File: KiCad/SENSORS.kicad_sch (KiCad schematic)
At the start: 0 parts

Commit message: Canvis a sensors
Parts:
- added D1: LED, symbol Device:LED
- added U1: TMP102xxDRL, Package_TO_SOT_SMD:SOT-563, symbol Sensor_Temperature:TMP102xxDRL
- added U2: A1104xLH, Package_TO_SOT_SMD:SOT-23W, symbol Sensor_Magnetic:A1104xLH
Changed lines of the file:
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@@
 	(generator_version "9.0")
 	(paper "A4")
+	(symbol
+		(lib_id "Sensor_Temperature:TMP102xxDRL")
+		(at 139.7 77.47 0)
+		(unit 1)
+		(exclude_from_sim no)
+		(in_bom yes)
+		(on_board yes)
+		(dnp no)
+		(fields_autoplaced yes)
+		(property "Reference" "U1"
+			(at 154.94 65.9698 0)
+			(effects
+				(font
+					(size 1.27 1.27)
+				)
+			)
+		)
+		(property "Value" "TMP102xxDRL"
+			(at 154.94 68.5098 0)
+			(effects
+				(font
+					(size 1.27 1.27)
+				)
+			)
+		)
+		(property "Footprint" "Package_TO_SOT_SMD:SOT-563"
+			(at 140.97 86.36 0)
+			(effects
+				(font
+					(size 1.27 1.27)
+				)
+				(justify left)
+				(hide yes)
+			)
+		)
+		(property "Datasheet" "https://www.ti.com/lit/ds/symlink/tmp102.pdf"
+			(at 140.97 88.9 0)
+			(effects
+				(font
+					(size 1.27 1.27)
+				)
+				(justify left)
+				(hide yes)
+			)
+		)
+		(property "Description" "Digital Temperature Sensor, ±3°C, low-Power, SMBus, 12 bit, Two-Wire Serial Interface, SOT-563"
+			(at 139.7 77.47 0)
+			(effects
+				(font
+					(size 1.27 1.27)
+				)
+				(hide yes)
+			)
+		)
+		(pin "4"
+		)
+		(pin "3"
+		)
+		(pin "5"
+		)
+		(pin "2"
+		)
+		(pin "1"
+		)
+		(pin "6"
+		)
+		(instances
+			(project ""
+				(path "/264905d4-7c45-4183-babb-a5b2177ba886"
+					(reference "U1")
+					(unit 1)
+				)
+			)
+		)
+	)
+	(symbol
+		(lib_id "Device:LED")
+		(at 166.37 107.95 0)
+		(unit 1)
+		(exclude_from_sim no)
+		(in_bom yes)
+		(on_board yes)
+		(dnp no)
+		(fields_autoplaced yes)
+		(property "Reference" "D1"
+			(at 164.7825 101.6 0)
+			(effects
+				(font
+					(size 1.27 1.27)
+				)
+			)
+		)
+		(property "Value" "LED"
+			(at 164.7825 104.14 0)
+			(effects
+				(font
+					(size 1.27 1.27)
+				)
+			)
+		)
+		(property "Footprint" ""
+			(at 166.37 107.95 0)
+			(effects
+				(font
+					(size 1.27 1.27)
+				)
+				(hide yes)
+			)
+		)
+		(property "Datasheet" "~"
+			(at 166.37 107.95 0)
+			(effects
+				(font
+					(size 1.27 1.27)
+				)
+				(hide yes)
+			)
+		)
+		(property "Description" "Light emitting diode"
+			(at 166.37 107.95 0)
+			(effects
+				(font
+					(size 1.27 1.27)
+				)
+				(hide yes)
+			)
+		)
+		(property "Sim.Pins" "1=K 2=A"
+			(at 166.37 107.95 0)
+			(effects
+				(font
+					(size 1.27 1.27)
+				)
+				(hide yes)
+			)
+		)
+		(pin "1"
+		)
+		(pin "2"
+		)
+		(instances
+			(project ""
+				(path "/264905d4-7c45-4183-babb-a5b2177ba886"
+					(reference "D1")
+					(unit 1)
+				)
+			)
+		)
+	)
+	(symbol
+		(lib_id "Sensor_Magnetic:A1104xLH")
+		(at 139.7 121.92 0)
+		(unit 1)
+		(exclude_from_sim no)
+		(in_bom yes)
+		(on_board yes)
+		(dnp no)
+		(fields_autoplaced yes)
+		(property "Reference" "U2"
+			(at 133.35 120.6499 0)
+			(effects
+				(font
+					(size 1.27 1.27)
+				)
+				(justify right)
+			)
+		)
+		(property "Value" "A1104xLH"
+			(at 133.35 123.1899 0)
+			(effects
+				(font
+					(size 1.27 1.27)
+				)
+				(justify right)
+			)
+		)
+		(property "Footprint" "Package_TO_SOT_SMD:SOT-23W"
+			(at 139.7 139.192 0)
+			(effects
+				(font
+					(size 1.27 1.27)
+					(italic yes)
+				)
+				(hide yes)
+			)
+		)
+		(property "Datasheet" "https://www.allegromicro.com/-/media/files/datasheets/a110x-datasheet.ashx"
+			(at 139.7 134.62 0)
+			(effects
+				(font
+					(size 1.27 1.27)
+				)
+				(hide yes)
+			)
+		)
+		(property "Description" "Hall effect switch, unipolar (south-polarity), Bop=70-350G, Brp=50-330G, 3.8-24V supply, SOT-23W"
+			(at 139.7 136.906 0)
+			(effects
+				(font
+					(size 1.27 1.27)
+				)
+				(hide yes)
+			)
+		)
+		(pin "2"
+		)
+		(pin "1"
+		)
+		(pin "3"
+		)
+		(instances
+			(project ""
+				(path "/264905d4-7c45-4183-babb-a5b2177ba886"
+					(reference "U2")
+					(unit 1)
+				)
+			)
+		)
+	)
+	(sheet_instances
+		(path "/"
+			(page "1")
+		)
+	)
+	(embedded_fonts no)
 )

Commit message: Canvis a SENSORS
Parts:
- added R1: R, symbol Device:R
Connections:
- net at D1.1 (K): now also R1.1
- net at U2.2 (V_{OUT}): now also R1.2
- net GND: now reaches U2.3 (GND)
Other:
- moved on the sheet: D1, U1
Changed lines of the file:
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@@
 	(generator_version "9.0")
 	(paper "A4")
+	(wire
+		(pts
+			(xy 147.32 121.92) (xy 152.4 121.92)
+		)
+		(stroke
+			(width 0)
+			(type default)
+		)
+	)
+	(wire
+		(pts
+			(xy 137.16 132.08) (xy 137.16 135.89)
+		)
+		(stroke
+			(width 0)
+			(type default)
+		)
+	)
+	(wire
+		(pts
+			(xy 152.4 121.92) (xy 152.4 115.57)
+		)
+		(stroke
+			(width 0)
+			(type default)
+		)
+	)
+	(wire
+		(pts
+			(xy 152.4 101.6) (xy 152.4 107.95)
+		)
+		(stroke
+			(width 0)
+			(type default)
+		)
+	)
 	(symbol
 		(lib_id "Sensor_Temperature:TMP102xxDRL")
-		(at 139.7 77.47 0)
+		(at 110.49 41.91 0)
 		(unit 1)
 		(exclude_from_sim no)
@@
 		(fields_autoplaced yes)
 		(property "Reference" "U1"
-			(at 154.94 65.9698 0)
+			(at 125.73 30.4098 0)
 			(effects
 				(font
@@
 		)
 		(property "Value" "TMP102xxDRL"
-			(at 154.94 68.5098 0)
+			(at 125.73 32.9498 0)
 			(effects
 				(font
@@
 		)
 		(property "Footprint" "Package_TO_SOT_SMD:SOT-563"
-			(at 140.97 86.36 0)
+			(at 111.76 50.8 0)
 			(effects
 				(font
@@
 		)
 		(property "Datasheet" "https://www.ti.com/lit/ds/symlink/tmp102.pdf"
-			(at 140.97 88.9 0)
+			(at 111.76 53.34 0)
 			(effects
 				(font
@@
 		)
 		(property "Description" "Digital Temperature Sensor, ±3°C, low-Power, SMBus, 12 bit, Two-Wire Serial Interface, SOT-563"
-			(at 139.7 77.47 0)
+			(at 110.49 41.91 0)
 			(effects
 				(font
@@
 	(symbol
 		(lib_id "Device:LED")
-		(at 166.37 107.95 0)
+		(at 152.4 97.79 90)
 		(unit 1)
 		(exclude_from_sim no)
@@
 		(fields_autoplaced yes)
 		(property "Reference" "D1"
-			(at 164.7825 101.6 0)
-			(effects
-				(font
-					(size 1.27 1.27)
-				)
+			(at 156.21 98.1074 90)
+			(effects
+				(font
+					(size 1.27 1.27)
+				)
+				(justify right)
 			)
 		)
 		(property "Value" "LED"
-			(at 164.7825 104.14 0)
-			(effects
-				(font
-					(size 1.27 1.27)
-				)
+			(at 156.21 100.6474 90)
+			(effects
+				(font
+					(size 1.27 1.27)
+				)
+				(justify right)
 			)
 		)
 		(property "Footprint" ""
-			(at 166.37 107.95 0)
+			(at 152.4 97.79 0)
 			(effects
 				(font
@@
 		)
 		(property "Datasheet" "~"
-			(at 166.37 107.95 0)
+			(at 152.4 97.79 0)
 			(effects
 				(font
@@
 		)
 		(property "Description" "Light emitting diode"
-			(at 166.37 107.95 0)
+			(at 152.4 97.79 0)
 			(effects
 				(font
@@
 		)
 		(property "Sim.Pins" "1=K 2=A"
-			(at 166.37 107.95 0)
+			(at 152.4 97.79 0)
 			(effects
 				(font
@@
 					(unit 1)
 				)
+			)
+		)
+	)
+	(symbol
+		(lib_id "Device:R")
+		(at 152.4 111.76 0)
+		(unit 1)
+		(exclude_from_sim no)
+		(in_bom yes)
+		(on_board yes)
+		(dnp no)
+		(fields_autoplaced yes)
+		(property "Reference" "R1"
+			(at 154.94 110.4899 0)
+			(effects
+				(font
+					(size 1.27 1.27)
+				)
+				(justify left)
+			)
+		)
+		(property "Value" "R"
+			(at 154.94 113.0299 0)
+			(effects
+				(font
+					(size 1.27 1.27)
+				)
+				(justify left)
+			)
+		)
+		(property "Footprint" ""
+			(at 150.622 111.76 90)
+			(effects
+				(font
+					(size 1.27 1.27)
+				)
+				(hide yes)
+			)
+		)
+		(property "Datasheet" "~"
+			(at 152.4 111.76 0)
+			(effects
+				(font
+					(size 1.27 1.27)
+				)
+				(hide yes)
+			)
+		)
+		(property "Description" "Resistor"
+			(at 152.4 111.76 0)
+			(effects
+				(font
+					(size 1.27 1.27)
+				)
+				(hide yes)
+			)
+		)
+		(pin "1"
+		)
+		(pin "2"
+		)
+		(instances
+			(project ""
+				(path "/264905d4-7c45-4183-babb-a5b2177ba886"
+					(reference "R1")
+					(unit 1)
+				)
+			)
+		)
+	)
+	(symbol
+		(lib_id "power:GND")
+		(at 137.16 135.89 0)
+		(unit 1)
+		(exclude_from_sim no)
+		(in_bom yes)
+		(on_board yes)
+		(dnp no)
+		(fields_autoplaced yes)
+		(property "Reference" "#PWR01"
+			(at 137.16 142.24 0)
+			(effects
+				(font
+					(size 1.27 1.27)
+				)
+				(hide yes)
+			)
+		)
+		(property "Value" "GND"
+			(at 137.16 140.97 0)
+			(effects
+				(font
+					(size 1.27 1.27)
+				)
+			)
+		)
+		(property "Footprint" ""
+			(at 137.16 135.89 0)
+			(effects
+				(font
+					(size 1.27 1.27)
+				)
+				(hide yes)
+			)
+		)
+		(property "Datasheet" ""
+			(at 137.16 135.89 0)
+			(effects
+				(font
+					(size 1.27 1.27)
+				)
+				(hide yes)
+			)
+		)
+		(property "Description" "Power symbol creates a global label with name \"GND\" , ground"
+			(at 137.16 135.89 0)
+			(effects
+				(font
+					(size 1.27 1.27)
+				)
+				(hide yes)
+			)
+		)
+		(pin "1"
+		)
+		(instances
+			(project ""
+				(path "/264905d4-7c45-4183-babb-a5b2177ba886"
+					(reference "#PWR01")
+					(unit 1)
+				)

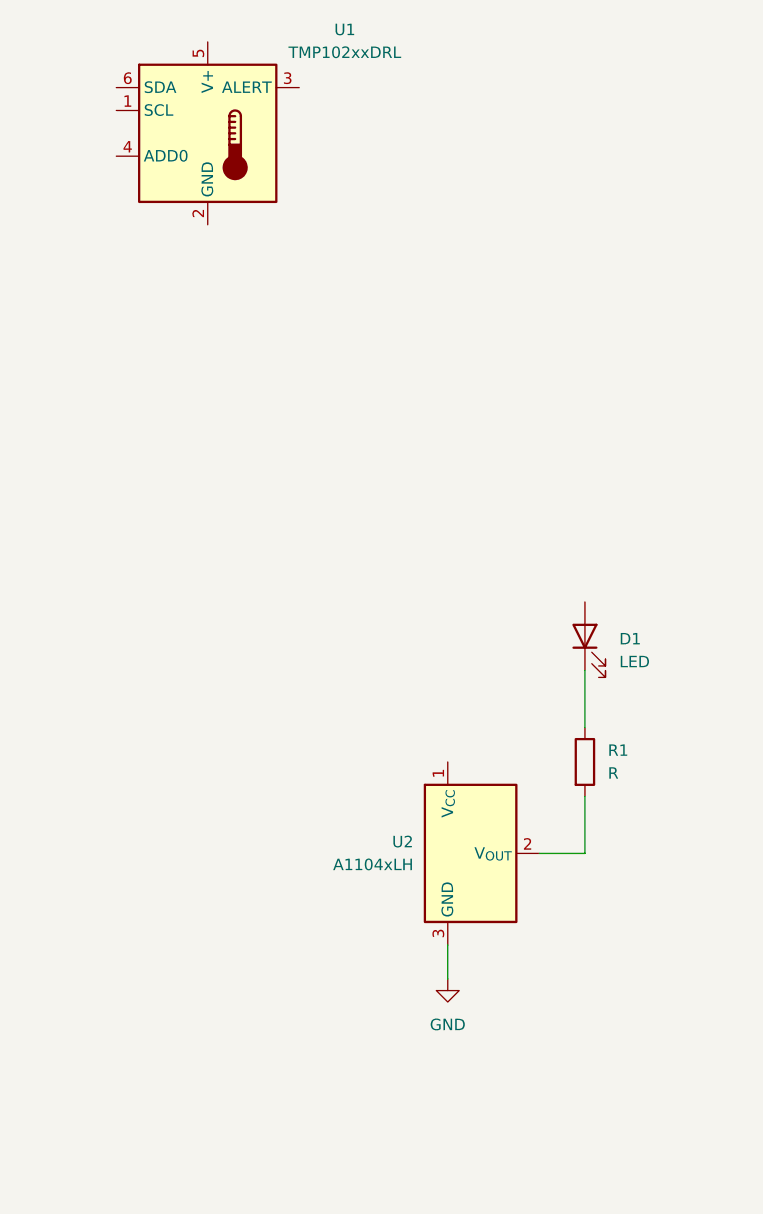
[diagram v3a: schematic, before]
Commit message: Canvis als SENSORS: fet al 70%
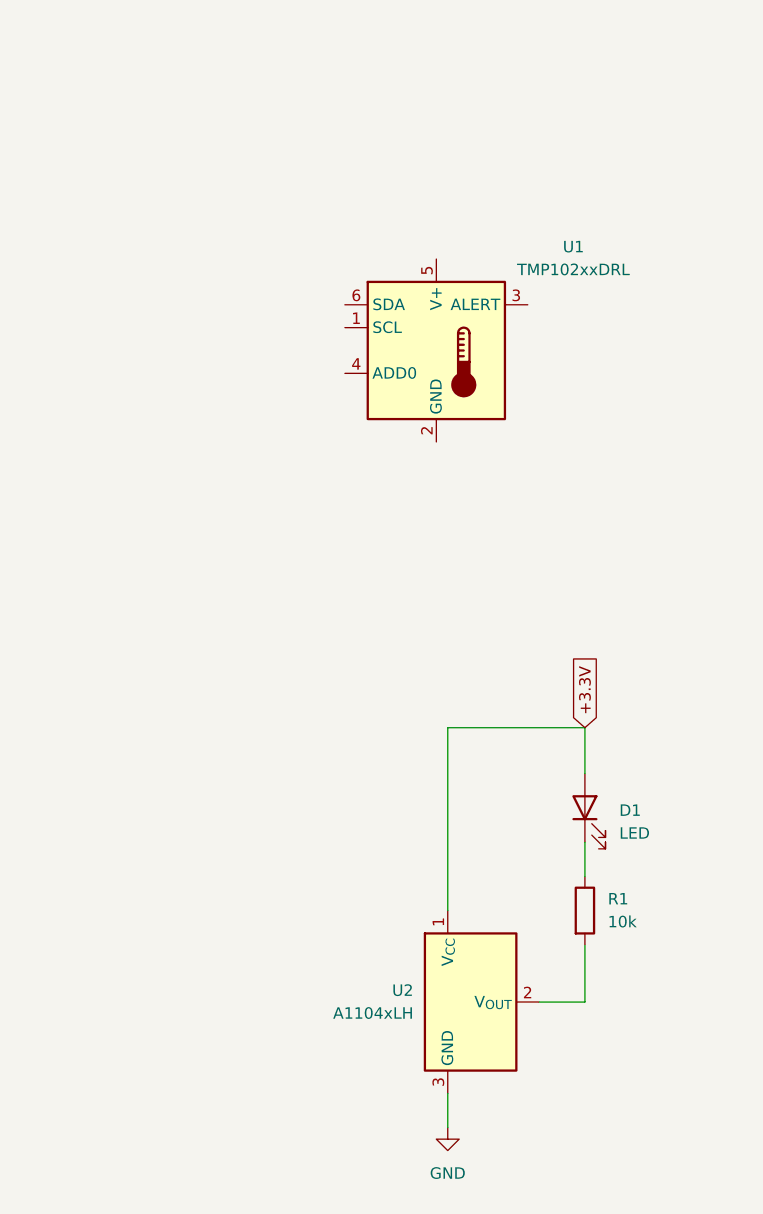
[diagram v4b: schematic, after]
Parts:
- R1: value R -> 10k
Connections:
- net +3.3V: now reaches D1.2 (A)
- net +3.3V: now also U2.1 (V_{CC})
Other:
- moved on the sheet: D1, R1, U1, U2
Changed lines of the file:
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@@
 	(wire
 		(pts
-			(xy 147.32 121.92) (xy 152.4 121.92)
-		)
-		(stroke
-			(width 0)
-			(type default)
-		)
-	)
-	(wire
-		(pts
-			(xy 137.16 132.08) (xy 137.16 135.89)
-		)
-		(stroke
-			(width 0)
-			(type default)
-		)
-	)
-	(wire
-		(pts
-			(xy 152.4 121.92) (xy 152.4 115.57)
-		)
-		(stroke
-			(width 0)
-			(type default)
-		)
-	)
-	(wire
-		(pts
-			(xy 152.4 101.6) (xy 152.4 107.95)
-		)
-		(stroke
-			(width 0)
-			(type default)
+			(xy 147.32 138.43) (xy 152.4 138.43)
+		)
+		(stroke
+			(width 0)
+			(type default)
+		)
+	)
+	(wire
+		(pts
+			(xy 137.16 107.95) (xy 152.4 107.95)
+		)
+		(stroke
+			(width 0)
+			(type default)
+		)
+	)
+	(wire
+		(pts
+			(xy 152.4 120.65) (xy 152.4 124.46)
+		)
+		(stroke
+			(width 0)
+			(type default)
+		)
+	)
+	(wire
+		(pts
+			(xy 137.16 148.59) (xy 137.16 152.4)
+		)
+		(stroke
+			(width 0)
+			(type default)
+		)
+	)
+	(wire
+		(pts
+			(xy 137.16 128.27) (xy 137.16 107.95)
+		)
+		(stroke
+			(width 0)
+			(type default)
+		)
+	)
+	(wire
+		(pts
+			(xy 152.4 138.43) (xy 152.4 132.08)
+		)
+		(stroke
+			(width 0)
+			(type default)
+		)
+	)
+	(wire
+		(pts
+			(xy 152.4 107.95) (xy 152.4 113.03)
+		)
+		(stroke
+			(width 0)
+			(type default)
+		)
+	)
+	(global_label "+3.3V"
+		(shape input)
+		(at 152.4 107.95 90)
+		(fields_autoplaced yes)
+		(effects
+			(font
+				(size 1.27 1.27)
+			)
+			(justify left)
+		)
+		(property "Intersheetrefs" "${INTERSHEET_REFS}"
+			(at 152.4 99.28 90)
+			(effects
+				(font
+					(size 1.27 1.27)
+				)
+				(justify left)
+				(hide yes)
+			)
 		)
 	)
 	(symbol
 		(lib_id "Sensor_Temperature:TMP102xxDRL")
-		(at 110.49 41.91 0)
+		(at 135.89 66.04 0)
 		(unit 1)
 		(exclude_from_sim no)
@@
 		(dnp no)
 		(fields_autoplaced yes)
-		(property "Reference" "U?"
-			(at 125.73 30.4098 0)
+		(property "Reference" "U1"
+			(at 151.13 54.5398 0)
 			(effects
 				(font
@@
 		)
 		(property "Value" "TMP102xxDRL"
-			(at 125.73 32.9498 0)
+			(at 151.13 57.0798 0)
 			(effects
 				(font
@@
 		)
 		(property "Footprint" "Package_TO_SOT_SMD:SOT-563"
-			(at 111.76 50.8 0)
+			(at 137.16 74.93 0)
 			(effects
 				(font
@@
 		)
 		(property "Datasheet" "https://www.ti.com/lit/ds/symlink/tmp102.pdf"
-			(at 111.76 53.34 0)
+			(at 137.16 77.47 0)
 			(effects
 				(font
@@
 		)
 		(property "Description" "Digital Temperature Sensor, ±3°C, low-Power, SMBus, 12 bit, Two-Wire Serial Interface, SOT-563"
-			(at 110.49 41.91 0)
+			(at 135.89 66.04 0)
 			(effects
 				(font
@@
 	(symbol
 		(lib_id "Device:LED")
-		(at 152.4 97.79 90)
+		(at 152.4 116.84 90)
 		(unit 1)
 		(exclude_from_sim no)
@@
 		(dnp no)
 		(fields_autoplaced yes)
-		(property "Reference" "D?"
-			(at 156.21 98.1074 90)
+		(property "Reference" "D1"
+			(at 156.21 117.1574 90)
 			(effects
 				(font
@@
 		)
 		(property "Value" "LED"
-			(at 156.21 100.6474 90)
+			(at 156.21 119.6974 90)
 			(effects
 				(font
@@
 		)
 		(property "Footprint" ""
-			(at 152.4 97.79 0)
+			(at 152.4 116.84 0)
 			(effects
 				(font
@@
 		)
 		(property "Datasheet" "~"
-			(at 152.4 97.79 0)
+			(at 152.4 116.84 0)
 			(effects
 				(font
@@
 		)
 		(property "Description" "Light emitting diode"
-			(at 152.4 97.79 0)
+			(at 152.4 116.84 0)
 			(effects
 				(font
@@
 		)
 		(property "Sim.Pins" "1=K 2=A"
-			(at 152.4 97.79 0)
+			(at 152.4 116.84 0)
 			(effects
 				(font
@@
 		)
 		(instances
-			(project ""
+			(project "SENSORS"
 				(path "/264905d4-7c45-4183-babb-a5b2177ba886"
 					(reference "D1")
@@
 				)
 			)
-			(project "SEIENTS_EDD"
-				(path "/b6401b4f-5426-49b8-bb2e-8ecdb19989ef/e4bd2572-b2cc-4f8d-9ea8-3fa488d49274"
-					(reference "D?")
-					(unit 1)
-				)
-			)
 		)
 	)
 	(symbol
 		(lib_id "Device:R")
-		(at 152.4 111.76 0)
+		(at 152.4 128.27 0)
 		(unit 1)
 		(exclude_from_sim no)
@@
 		(dnp no)
 		(fields_autoplaced yes)
-		(property "Reference" "R?"
-			(at 154.94 110.4899 0)
+		(property "Reference" "R1"
+			(at 154.94 126.9999 0)
 			(effects
 				(font
@@
 			)
 		)
-		(property "Value" "R"
-			(at 154.94 113.0299 0)
+		(property "Value" "10k"
+			(at 154.94 129.5399 0)
 			(effects
 				(font
@@
 		)
 		(property "Footprint" ""
-			(at 150.622 111.76 90)
+			(at 150.622 128.27 90)
 			(effects
 				(font
@@
 		)
 		(property "Datasheet" "~"
-			(at 152.4 111.76 0)
+			(at 152.4 128.27 0)
 			(effects
 				(font
@@
 		)
 		(property "Description" "Resistor"
-			(at 152.4 111.76 0)
+			(at 152.4 128.27 0)
 			(effects
 				(font
@@
 	(symbol
 		(lib_id "power:GND")
-		(at 137.16 135.89 0)
+		(at 137.16 152.4 0)
 		(unit 1)
 		(exclude_from_sim no)
@@
 		(dnp no)
 		(fields_autoplaced yes)
-		(property "Reference" "#PWR?"
-			(at 137.16 142.24 0)
+		(property "Reference" "#PWR01"
+			(at 137.16 158.75 0)
 			(effects
 				(font
@@
 		)
 		(property "Value" "GND"
-			(at 137.16 140.97 0)
+			(at 137.16 157.48 0)
 			(effects
 				(font
@@
 		)
 		(property "Footprint" ""
-			(at 137.16 135.89 0)
+			(at 137.16 152.4 0)
 			(effects
 				(font
@@
 		)
 		(property "Datasheet" ""
-			(at 137.16 135.89 0)
+			(at 137.16 152.4 0)
 			(effects
 				(font
@@
 		)
 		(property "Description" "Power symbol creates a global label with name \"GND\" , ground"
-			(at 137.16 135.89 0)
+			(at 137.16 152.4 0)
 			(effects
 				(font
@@
 	(symbol
 		(lib_id "Sensor_Magnetic:A1104xLH")
-		(at 139.7 121.92 0)
+		(at 139.7 138.43 0)
 		(unit 1)
 		(exclude_from_sim no)
@@
 		(dnp no)
 		(fields_autoplaced yes)
-		(property "Reference" "U?"
-			(at 133.35 120.6499 0)
+		(property "Reference" "U2"
+			(at 133.35 137.1599 0)
 			(effects
 				(font
@@
 		)
 		(property "Value" "A1104xLH"
-			(at 133.35 123.1899 0)
+			(at 133.35 139.6999 0)
 			(effects
 				(font
@@
 		)
 		(property "Footprint" "Package_TO_SOT_SMD:SOT-23W"
-			(at 139.7 139.192 0)
+			(at 139.7 155.702 0)
 			(effects
 				(font
@@
 		)
 		(property "Datasheet" "https://www.allegromicro.com/-/media/files/datasheets/a110x-datasheet.ashx"
-			(at 139.7 134.62 0)
+			(at 139.7 151.13 0)
 			(effects
 				(font
@@
 		)
 		(property "Description" "Hall effect switch, unipolar (south-polarity), Bop=70-350G, Brp=50-330G, 3.8-24V supply, SOT-23W"
-			(at 139.7 136.906 0)
-			(effects
-				(font
+			(at 139.7 153.416 0)
+			(effects
+				(font

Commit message: Canvis als SENSORS: fet al 90%
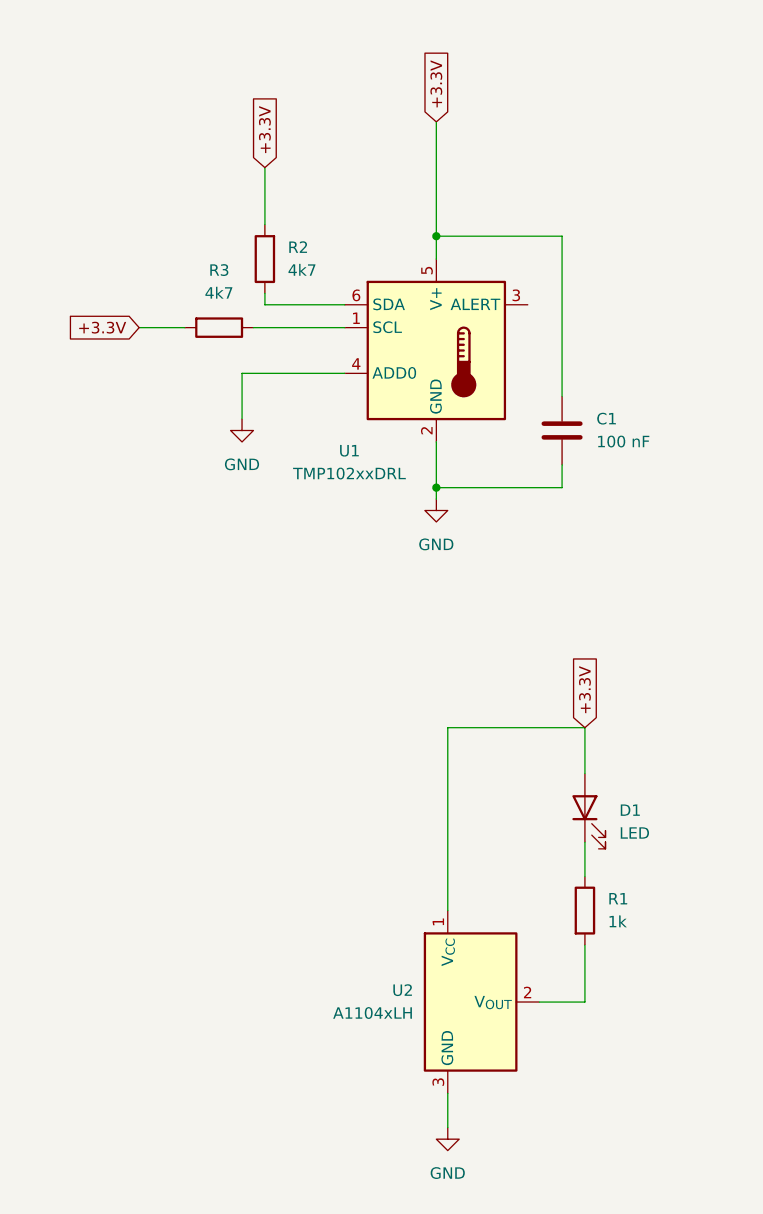
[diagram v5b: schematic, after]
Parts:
- added C1: 100 nF, symbol Device:C
- added R2, R3: 4k7, symbol Device:R
- R1: value 10k -> 1k
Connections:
- net +3.3V: now also U1.5 (V+), C1.1, R2.2, R3.2
- net GND: now also U1.2 (GND), U1.4 (ADD0), C1.2
- net at U1.1 (SCL): now also R3.1
- net at U1.6 (SDA): now also R2.1

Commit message: Canvis als SENSORS: Sensors acabats
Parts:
- added R4: 10k, symbol Device:R
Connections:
- net +3.3V: now also R2.1, R3.1, R4.1; no longer R2.2, R3.2
- net I2C_SCL: now reaches U1.1 (SCL)
- net I2C_SCL: now also R3.2; no longer R3.1
- net at U1.3 (ALERT): now also R4.2
- net I2C_SDA: now reaches U1.6 (SDA)
- net I2C_SDA: now also R2.2; no longer R2.1
- net HALL_OUT: now reaches R1.2, U2.2 (V_{OUT})
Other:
- moved on the sheet: R2, R3

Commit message: Modificació
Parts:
- renumbered C1 to C9, D1 to D3, R2 to R10, R3 to R11, R1 to R12, R4 to R13, U1 to U5, U2 to U6
